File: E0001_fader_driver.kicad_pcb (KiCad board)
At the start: 4 copper layers, 107 x 17 mm, 34 parts, among them J1 JST GH SM04B-GHS-TB, J2 TC2030-IDC-NL, Q1 AO3401A, U1 STM32C051F6P6, U2 MCP1703A-3302E/CB, U3 DRV8210PDSGR

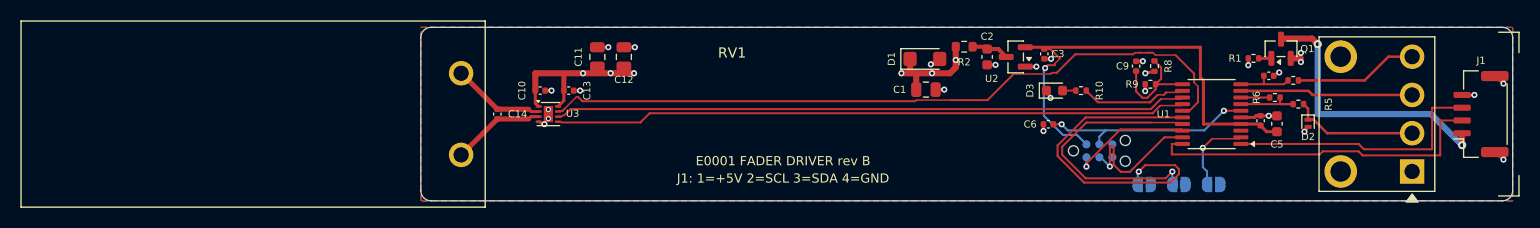
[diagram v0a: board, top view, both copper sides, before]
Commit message: Apply rev B layout/routing QC fixes
- ADDR0/ADDR1: via under U1, direct B.Cu runs to JP1/JP2 (detour 4.3x -> 1.3x);
  NRST B.Cu moved above the ADDR vias; SWCLK hairpin around J2 removed
- MOT_nSLEEP runs alongside IN1/IN2 (70.8 -> 63.0 mm), B.Cu crossover at U3
- Uniform 0.2 mm signal widths, 0.3 mm +3V3 trunk, tidied +5V widths
- Removed 15 snapping stubs, 5 acute corners and all off-45 deg segments
- 6 GND stitching vias near U3 and along the motor-control bundle
- Silkscreen to JLC minimums (1.0 mm / 0.15 mm); RV1 silk pulled inside
  the board edge (board and Fader library updated together)
- Add JLCPCB 4-layer .kicad_dru; DRC: 0 errors/warnings, 0 unconnected,
  0 parity issues

Co-Authored-By: Claude Opus 5.5 <noreply@anthropic.com>
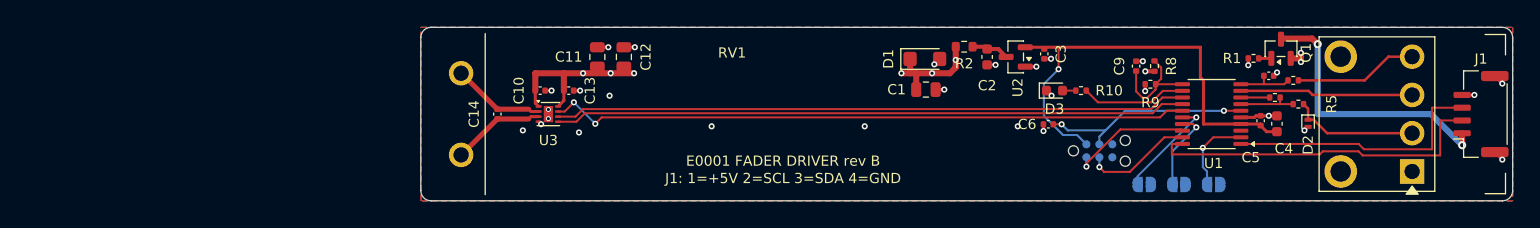
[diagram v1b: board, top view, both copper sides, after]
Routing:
- net /ADDR0: track 33.9 -> 10.3 mm
- net /ADDR1: track 26.9 -> 8.07 mm
- net /MOT_nSLEEP: track 70.8 -> 63.0 mm, vias 0 -> 2
- net /SWCLK: track 14.1 -> 10.7 mm
- net +3V3: track 48.3 -> 45.3 mm
- net /TOUCH_SNS: track 7.06 -> 5.78 mm
- net GND: track 20.2 -> 19.1 mm, vias 23 -> 29

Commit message: Layout QC round 2: acid traps, I2C reroute around fader touch pad
- +3V3 trunk runs through C3 pad 1 centre; NRST C6 branch and VSENSE R8
  feed now join at 90 deg instead of 45 deg wedges
- I2C: straight parallel SCL/SDA pair from U1 (no jog around FG, no hook
  at pin 20), dropping between FG and RV1 pad 1 and rising into J1 at
  x 166.8/167.25; edge gap to touch pad T 0.28 -> 1.85 mm, GND pour now
  fills around pad T. ADDR2 via moved under the U1 body to make room
- Chamfered right angles on +3V3, VIN, +5V, LDO_IN and TOUCH_ELEC;
  SWDIO aligned to U1 pin 18
- DRC (JLC rules): 0 violations, 0 unconnected, 0 parity issues

Co-Authored-By: Claude Opus 5.5 <noreply@anthropic.com>
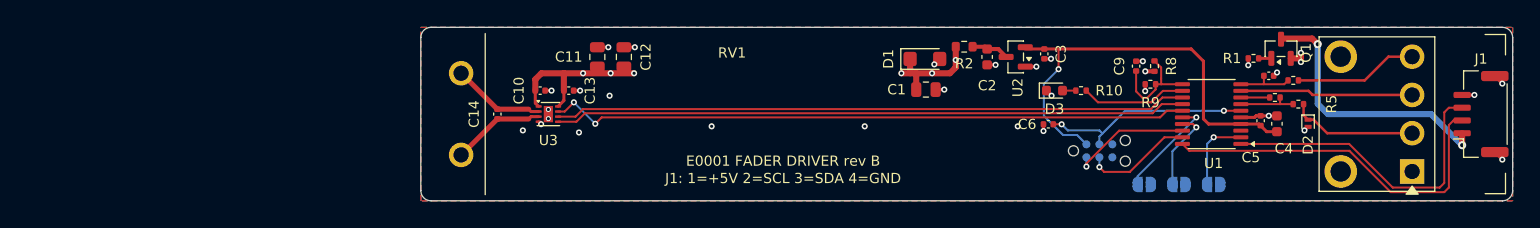
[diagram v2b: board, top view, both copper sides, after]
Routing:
- net /I2C_SDA: track 26.0 -> 30.8 mm
- net /I2C_SCL: track 34.2 -> 35.9 mm
- net +3V3: track 45.3 -> 43.8 mm
- net /VIN: track 27.3 -> 26.7 mm

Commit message: Hand-route experiment: strip rev B, scripted pre-route + Freerouting
All tracks and vias of the rev B board removed; placement, zones and
net classes unchanged. Own scripts (build/hr) pre-route the motor loop,
U3 supply, TOUCH_ELEC and a plane via for every GND/+5V SMD pad; the
remaining signal nets are routed by Freerouting 2.5.0 (DSN exported by
pcbnew, inner layers as power planes, keepout ring around the touch pad
for the I2C gap). Not TraceMaker. Joins not yet cleaned.

Co-Authored-By: Claude Opus 5.5 <noreply@anthropic.com>
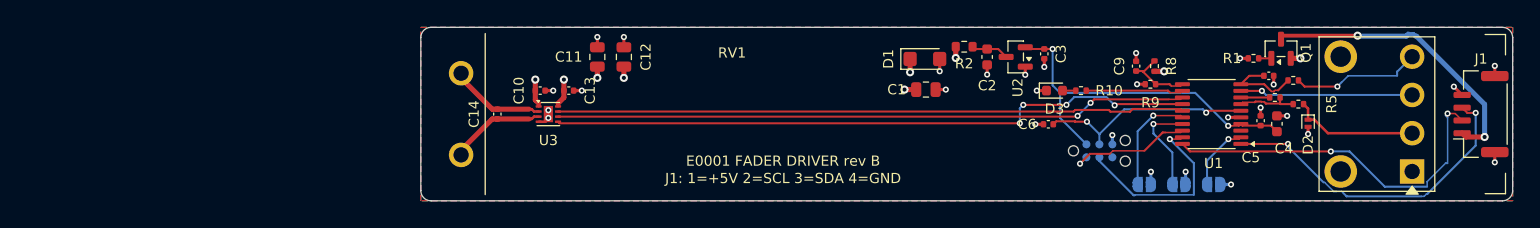
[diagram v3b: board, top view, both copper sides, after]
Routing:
- net +5V: track 29.6 -> 13.3 mm
- net /SWCLK: track 10.7 -> 18.8 mm
- net +3V3: track 43.8 -> 36.4 mm, vias 1 -> 2
- net GND: track 19.1 -> 26.3 mm, vias 29 -> 28
- net /VSENSE: track 10.2 -> 6.76 mm
- net /FADER_POS: track 5.61 -> 7.97 mm
- net /VIN: track 26.7 -> 28.8 mm
- net /MOT_IN2: track 61.9 -> 63.6 mm, vias 0 -> 4
- net /ADDR1: track 8.07 -> 9.53 mm
- net /MOT_nSLEEP: track 63.0 -> 61.5 mm, vias 2 -> 0
- net /I2C_SDA: track 30.8 -> 32.1 mm, vias 0 -> 2
- net /ADDR2: track 7.56 -> 6.60 mm
- net /LED: track 10.4 -> 9.59 mm
- net /FADER_WIPER: track 12.1 -> 12.8 mm, vias 0 -> 1
- net /I2C_SCL: track 35.9 -> 35.7 mm, vias 0 -> 2
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
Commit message: Hand-route experiment: DRC clean, no T-joins or right angles
Own cleanup pass (build/hr/cleanup.py) rebuilds Freerouting's chains as
45-degree paths and chamfers right angles; hand edits (fixes.py,
fixes2.py) daisy-chain +3V3, NRST, TOUCH_SNS, VSENSE and FADER_POS
through pads instead of T-joins, straighten I2C and VIN (0.5 mm all the
way), and keep TOUCH_ELEC 2.7 mm from I2C.

kicad-cli DRC with parity and refill: 0 violations, 0 unconnected,
0 parity. tm_viapad 0, slots 0, corners 0.

Co-Authored-By: Claude Opus 5.5 <noreply@anthropic.com>
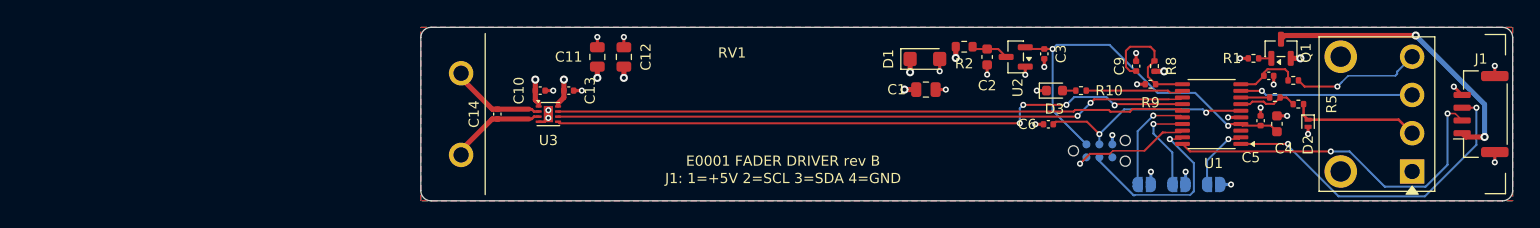
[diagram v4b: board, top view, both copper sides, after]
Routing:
- net /VSENSE: track 6.76 -> 12.4 mm
- net +3V3: track 36.4 -> 39.3 mm
- net /FADER_POS: track 7.97 -> 6.34 mm
